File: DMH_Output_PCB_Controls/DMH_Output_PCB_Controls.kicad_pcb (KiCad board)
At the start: 2 copper layers, 48 x 121 mm, 90 parts, among them J10 Conn_01x06, J11 Conn_01x06_PinHeader, J12 Conn_01x06_PinHeader, J13 Conn_01x06, J21 Conn_01x02, J22 Conn_01x02, Q1 BC558, Q2 BC558, U2 LM339, U21 LM4040LP-10, U24 LM339, U25 LM339, U3 LM339, U4 LM339, U5 LM339, U6 LM339

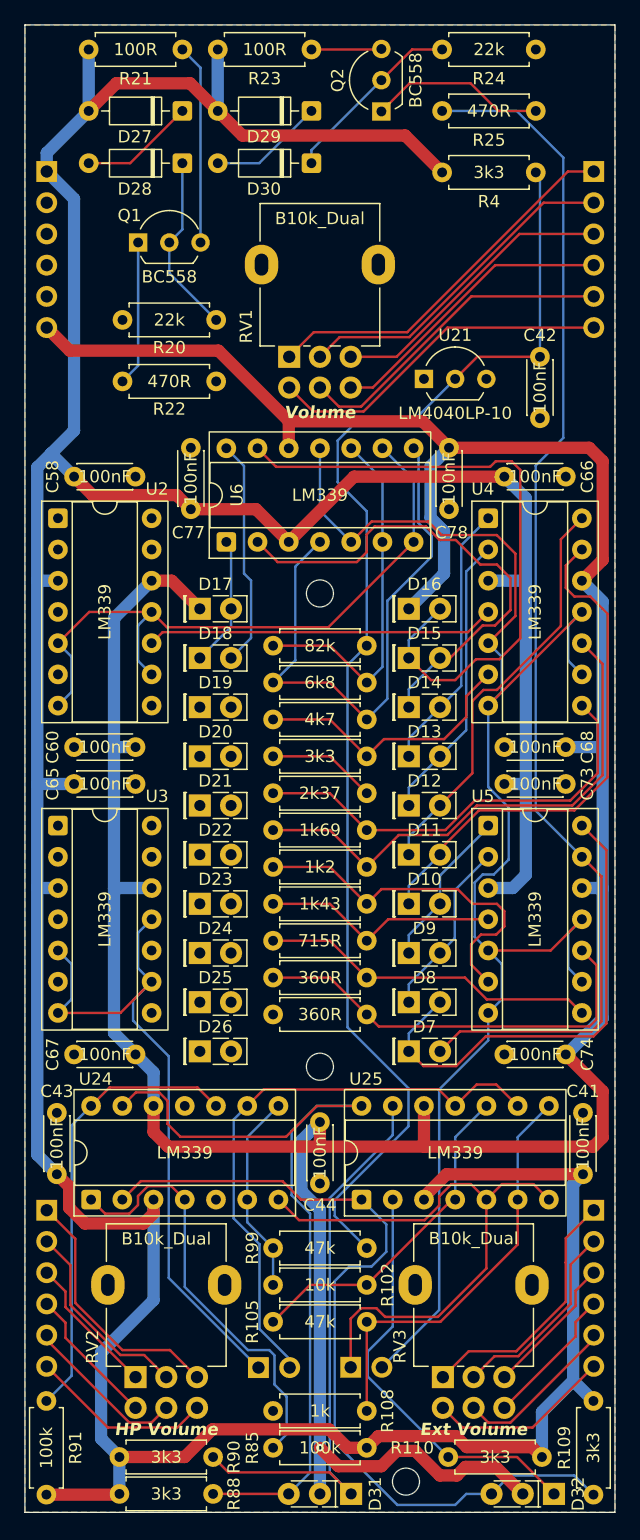
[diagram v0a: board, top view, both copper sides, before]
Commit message: Controls PCB Routing done
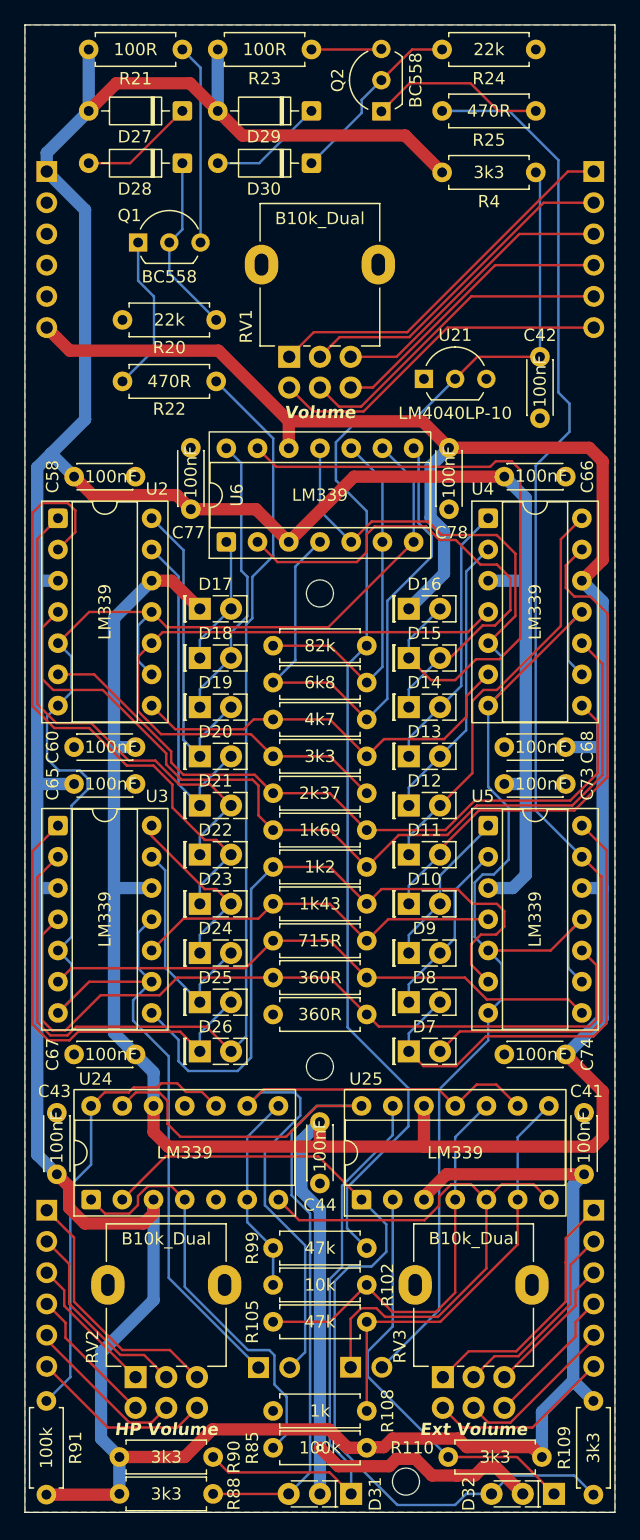
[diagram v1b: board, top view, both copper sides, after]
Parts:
- moved C41 0.09 mm to (96.5, 136.0)
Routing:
- net Net-(D26-A): track 0.00 -> 89.3 mm
- net Net-(D22-A): track 0.00 -> 50.9 mm
- net Net-(D21-A): track 0.00 -> 40.0 mm
- net Net-(D25-A): track 0.00 -> 37.2 mm
- net Net-(U2A--): track 42.6 -> 74.4 mm
- net Net-(U3A--): track 34.3 -> 64.4 mm
- net Net-(U3D--): track 29.5 -> 57.2 mm
- net Net-(D20-A): track 0.00 -> 27.5 mm
- net Net-(D19-A): track 0.00 -> 26.0 mm
- net Output_Meter_L_C: track 110.9 -> 134.6 mm
- net Net-(U2B--): track 35.6 -> 57.6 mm
- net Net-(U3B--): track 27.6 -> 46.4 mm
- net Net-(D24-A): track 0.00 -> 18.5 mm
- net Net-(U2C--): track 37.3 -> 55.8 mm
- net Net-(D23-A): track 0.00 -> 14.6 mm
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
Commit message: Created Main PCB project
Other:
- board text added: "Mk1.0 March 2026"
- board text removed: "Mk1.0 Month Year"
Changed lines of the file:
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@@
 		(layer "User.9")
 	)
-	(gr_text "Mk1.0\nMonth Year"
+	(gr_text "Mk1.0\nMarch 2026"
 		(at 53 73 270)
 		(layer "B.SilkS")

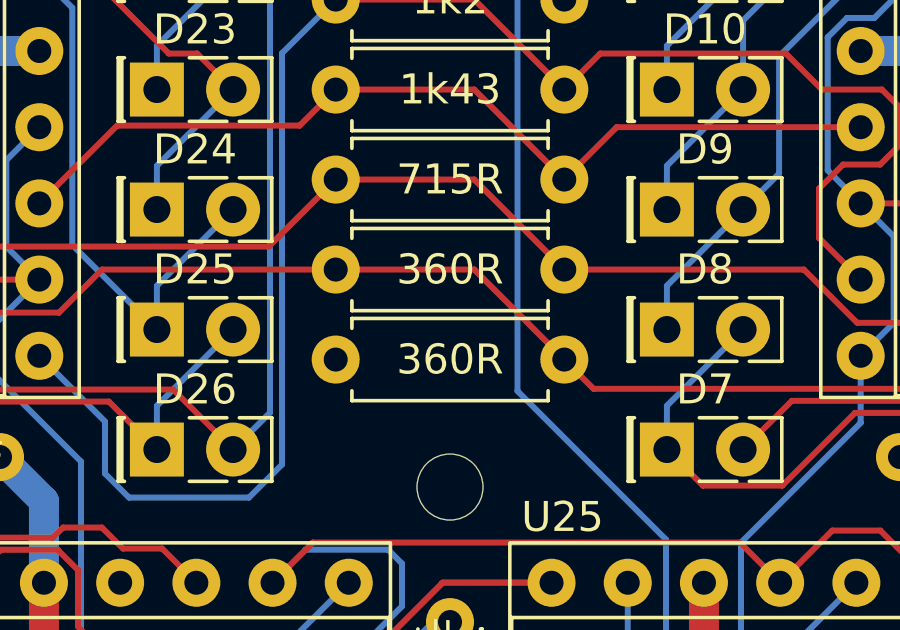
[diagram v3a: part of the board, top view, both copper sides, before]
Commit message: Adjustments during prototyping
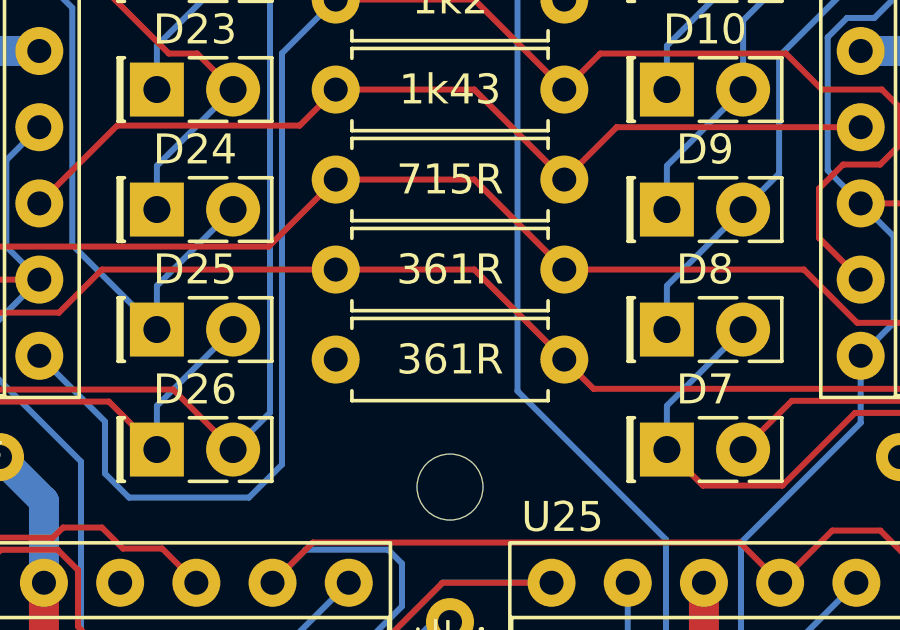
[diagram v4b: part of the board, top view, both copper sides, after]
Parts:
- R18, R19: value 360R -> 361R
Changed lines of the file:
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@@
 			)
 		)
-		(property "Value" "360R"
+		(property "Value" "361R"
 			(at 3.81 0 0)
 			(layer "F.SilkS")
@@
 			)
 		)
-		(property "Value" "360R"
+		(property "Value" "361R"
 			(at 3.81 0 0)
 			(layer "F.SilkS")

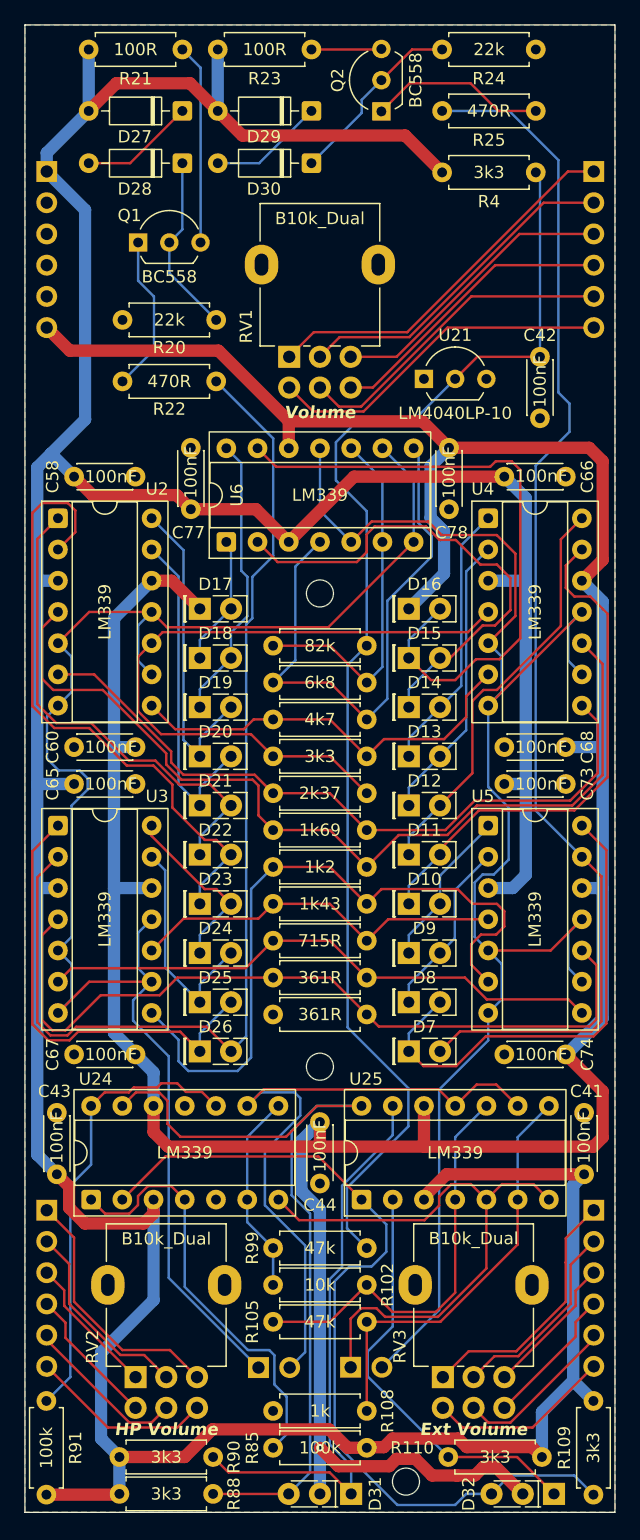
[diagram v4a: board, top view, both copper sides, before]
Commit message: Replaced jack symbols with 5pin ones
Also updated Meter LED current source resistor to 75R
Also increased LED guiding PCB mounting holes to M2.5
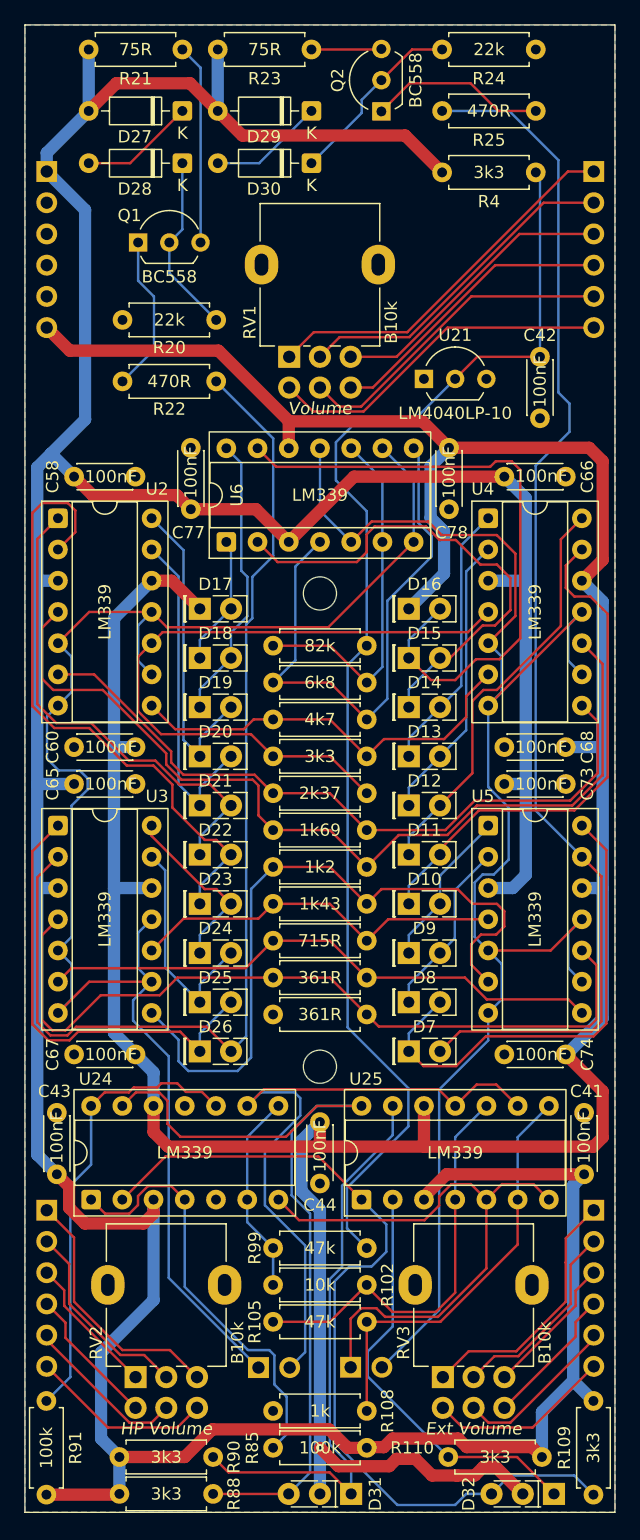
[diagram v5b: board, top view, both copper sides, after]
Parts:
- removed H23: MountingHole, MountingHole:MountingHole_2.2mm_M2
- H21, H22: footprint MountingHole:MountingHole_2.2mm_M2 -> MountingHole:MountingHole_2.7mm_M2.5_ISO14580
- R21, R23: value 100R -> 75R
- RV1, RV2, RV3: value B10k_Dual -> B10k; footprint Potentiometer_THT:Potentiometer_Alpha_RD902F-40-00D_Dual_Vertical -> SynthStuff:Potentiometer_Alpha_RD902F-40-00D_Dual_Vertical
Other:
- board text added: "Mk1.1 April 2026"
- board text removed: "Mk1.0 March 2026"
